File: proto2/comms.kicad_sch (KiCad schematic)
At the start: 35 parts

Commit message: Changes suggested by CFL.
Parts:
- C100, C101, C102, C103, C86, C87, C88, C89, C90, C91, C92, C93, C94, C95, C96, C97, C98, C99: renamed from C?; footprint (none) -> Capacitor_SMD:C_0805_2012Metric; LCSC (none) -> C440198
- U17: renamed from U?; Manufacturer (none) -> Texas Instruments; Part Number (none) -> ISO1540DR
- U18, U19, U20: renamed from U?; Manufacturer (none) -> Novosense; Part Number (none) -> NSI8021N-DSPR
- gave numbers to parts that had none: 13
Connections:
- net 3V3_I2C: now also R138.1
- net +5V renamed +5VP
- net +5VP: no longer C101.1, C93.1, C97.1, U18.1 (VDD1), U19.1 (VDD1), U20.1 (VDD1)
- new net +3V3: C101.1, C93.1, U18.1 (VDD1), U19.1 (VDD1), U20.1 (VDD1)

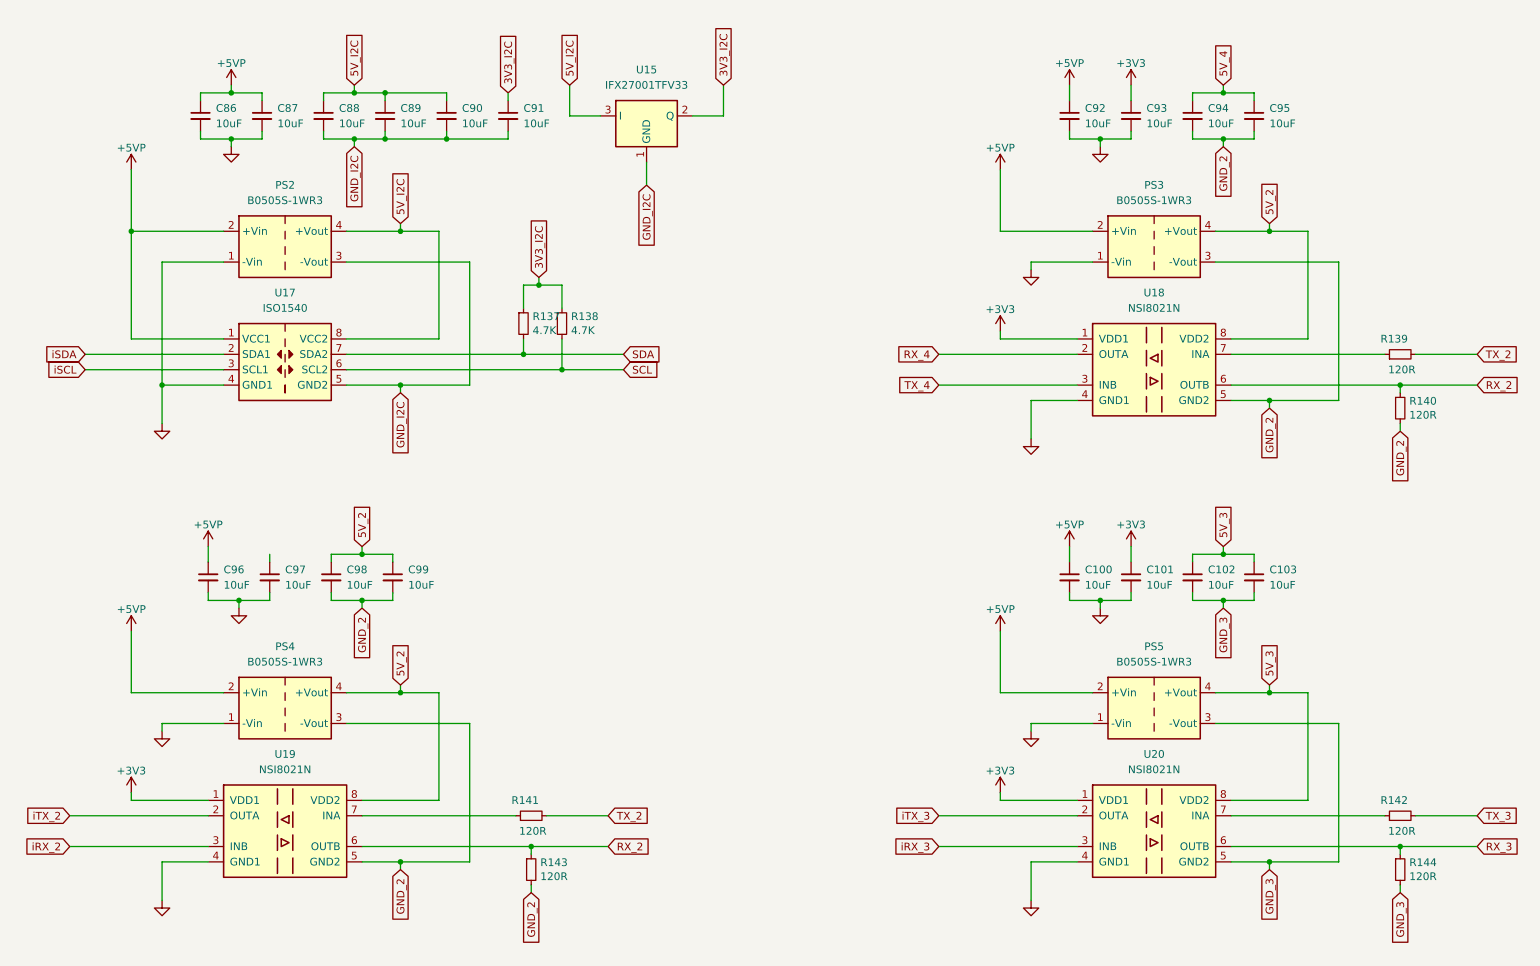
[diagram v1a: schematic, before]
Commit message: Laying out new filters and some schematic updates.
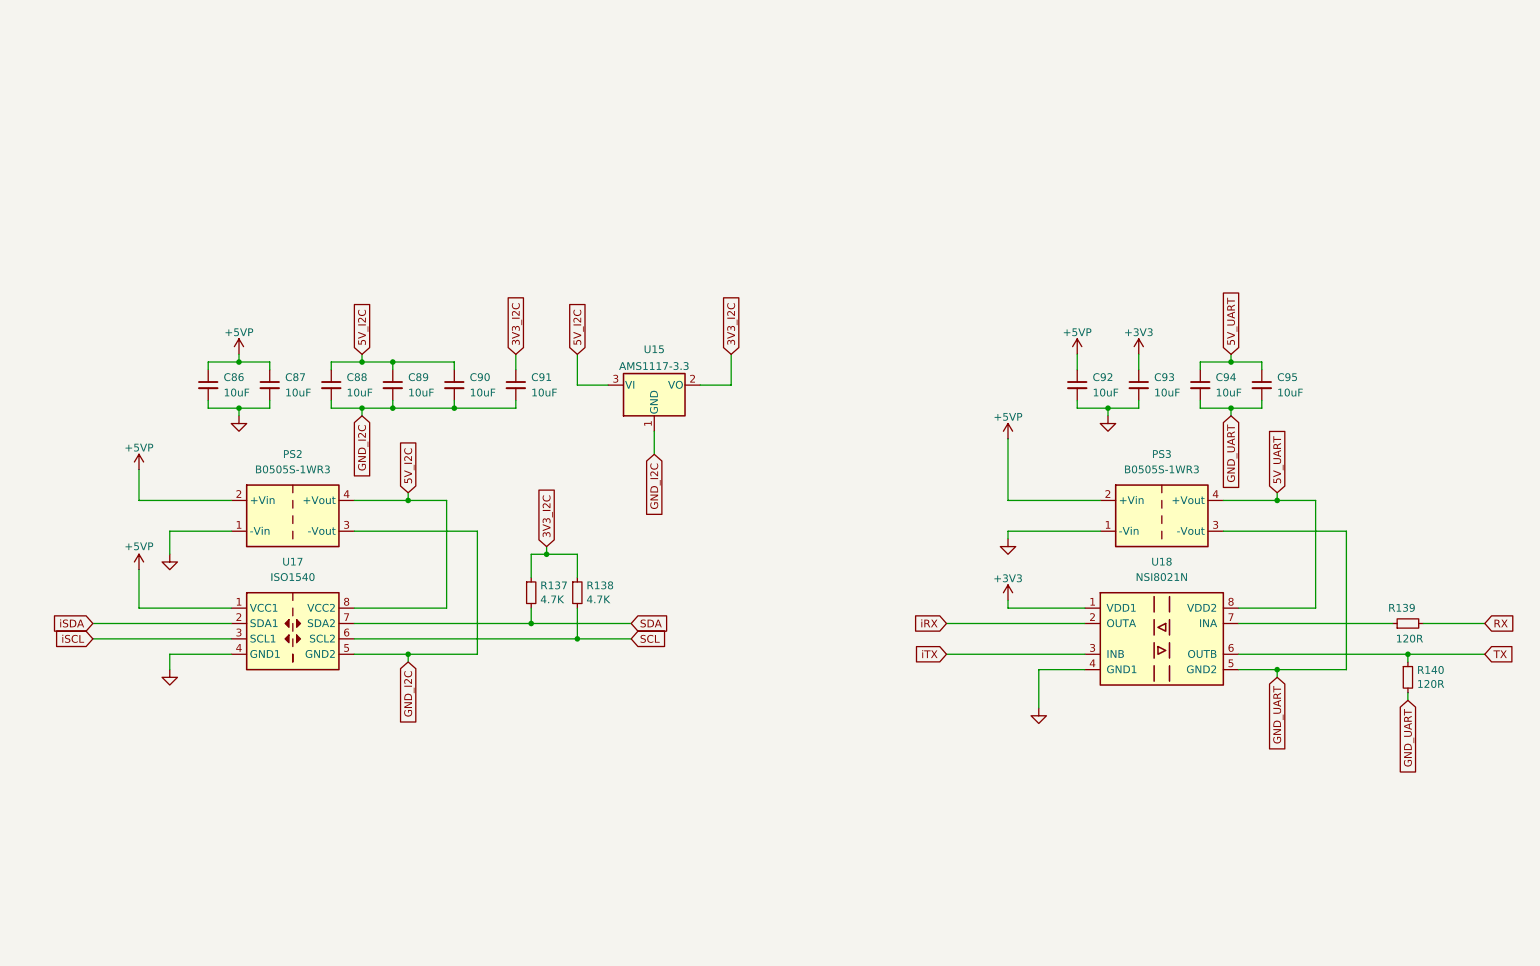
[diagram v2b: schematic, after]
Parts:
- removed C100, C101, C102, C103, C96, C97, C98, C99: 10uF, Capacitor_SMD:C_0805_2012Metric, symbol Device:C_Small
- removed PS4, PS5: B0505S-1WR3, Converter_DCDC:Converter_DCDC_Murata_MEE1SxxxxSC_THT, symbol Converter_DCDC:MEE1S0303SC
- removed R141, R142, R143, R144: 120R, Resistor_SMD:R_0805_2012Metric, symbol Device:R_Small
- removed U15: IFX27001TFV33, Package_TO_SOT_SMD:TO-252-3_TabPin2, symbol Regulator_Linear:IFX27001TFV33
- removed U19, U20: NSI8021N, Package_SO:SOIC-8_3.9x4.9mm_P1.27mm, symbol BCR:NSI8021N
- added U15: AMS1117-3.3, Package_TO_SOT_SMD:SOT-223-3_TabPin2, symbol Regulator_Linear:AMS1117-3.3
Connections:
- net 5V_4 is gone; now on net 5V_UART: C94.1, C95.1
- net 3V3_I2C: now also U15.2 (VO)
- net 5V_I2C: now also U15.3 (VI)
- net GND_I2C: now also U15.1 (GND)
- net 5V_2 renamed 5V_UART
- net GND renamed GND-SIG
- net GND_2 renamed GND_UART
- net RX_2 renamed TX
- net RX_4 renamed iRX
- net TX_2 renamed RX
- net TX_4 renamed iTX
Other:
- company: (none) -> Langhe Greenhaus
- title: (none) -> Greenhouse 2.0 IO Board
- moved on the sheet: C86, C87, C88, C89, C90, C91, C92, C93, C94, C95, PS2, PS3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

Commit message: Final layout for 0.2.0 and various BOM and minor schematic updates.
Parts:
- PS2, PS3: Manufacturer (none) -> Mornsun; Part Number (none) -> B0505S-1WR3
- U15: footprint Package_TO_SOT_SMD:SOT-223-3_TabPin2 -> JLCPCB:SOT-223-3; symbol Regulator_Linear:AMS1117-3.3 -> JLCPCB:AMS1117
- U17: footprint Package_SO:SOIC-8_3.9x4.9mm_P1.27mm -> JLCPCB:SOIC-8_5.4mm_1.27mm; symbol Isolator:ISO1540 -> JLCPCB:Taxas_ISO1540DR
- U18: footprint Package_SO:SOIC-8_3.9x4.9mm_P1.27mm -> JLCPCB:SOIC-8_5.4mm_1.27mm; symbol BCR:NSI8021N -> JLCPCB:Novosense_NSI8021N1-DSPR
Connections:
- no-connect marks 0 -> 1
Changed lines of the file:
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@@
   (junction (at 85.09 68.58) (diameter 0) (color 0 0 0 0)
   )
+  (no_connect (at 135.89 74.93))
   (wire (pts (xy 54.61 68.58) (xy 59.69 68.58))
     (stroke (width 0) (type default) (color 0 0 0 0))
@@
     (pin "2")
   )
-  (symbol (lib_id "Isolator:ISO1540") (at 68.58 111.76 0) (unit 1)
-    (in_bom yes) (on_board yes) (fields_autoplaced)
-    (property "Reference" "U17" (id 0) (at 68.58 101.6 0))
-    (property "Value" "ISO1540" (id 1) (at 68.58 104.14 0))
-    (property "Footprint" "Package_SO:SOIC-8_3.9x4.9mm_P1.27mm" (id 2) (at 68.58 120.65 0)
-      (effects (font (size 1.27 1.27)) hide)
-    )
-    (property "Datasheet" "https://datasheet.lcsc.com/lcsc/1811082013_Texas-Instruments-ISO1540DR_C179739.pdf" (id 3) (at 68.58 110.49 0)
-      (effects (font (size 1.27 1.27)) hide)
-    )
-    (property "LCSC" "C179739" (id 4) (at 68.58 111.76 0)
+  (symbol (lib_id "JLCPCB:Taxas_ISO1540DR") (at 68.58 111.76 0) (unit 1)
+    (in_bom yes) (on_board yes) (fields_autoplaced)
+    (property "Reference" "U17" (id 0) (at 68.58 102.9802 0))
+    (property "Value" "ISO1540" (id 1) (at 68.58 105.5171 0))
+    (property "Footprint" "JLCPCB:SOIC-8_5.4mm_1.27mm" (id 2) (at 68.58 120.65 0)
+      (effects (font (size 1.27 1.27)) hide)
+    )
+    (property "Datasheet" "https://datasheet.lcsc.com/lcsc/1811082013_Texas-Instruments-ISO1540DR_C179739.pdf" (id 3) (at 68.58 123.19 0)
+      (effects (font (size 1.27 1.27)) hide)
+    )
+    (property "LCSC" "C179739" (id 4) (at 68.58 125.73 0)
       (effects (font (size 1.27 1.27)) hide)
     )
@@
     )
     (property "Part Number" "ISO1540DR" (id 6) (at 68.58 111.76 0)
+      (effects (font (size 1.27 1.27)) hide)
+    )
+    (property "MPN" "" (id 7) (at 68.58 111.76 0)
+      (effects (font (size 1.27 1.27)) hide)
+    )
+    (property "JLC" "" (id 8) (at 68.58 111.76 0)
       (effects (font (size 1.27 1.27)) hide)
     )
@@
       (effects (font (size 1.27 1.27)) hide)
     )
+    (property "Manufacturer" "Mornsun" (id 5) (at 68.58 93.98 0)
+      (effects (font (size 1.27 1.27)) hide)
+    )
+    (property "Part Number" "B0505S-1WR3" (id 6) (at 68.58 93.98 0)
+      (effects (font (size 1.27 1.27)) hide)
+    )
     (pin "1")
     (pin "2")
@@
       (effects (font (size 1.27 1.27)) hide)
     )
+    (property "Manufacturer" "Mornsun" (id 5) (at 212.09 93.98 0)
+      (effects (font (size 1.27 1.27)) hide)
+    )
+    (property "Part Number" "B0505S-1WR3" (id 6) (at 212.09 93.98 0)
+      (effects (font (size 1.27 1.27)) hide)
+    )
     (pin "1")
     (pin "2")
@@
     (pin "1")
   )
-  (symbol (lib_id "BCR:NSI8021N") (at 212.09 114.3 0) (unit 1)
+  (symbol (lib_id "JLCPCB:Novosense_NSI8021N1-DSPR") (at 212.09 114.3 0) (unit 1)
     (in_bom yes) (on_board yes) (fields_autoplaced)
     (property "Reference" "U18" (id 0) (at 212.09 101.6 0))
     (property "Value" "NSI8021N" (id 1) (at 212.09 104.14 0))
-    (property "Footprint" "Package_SO:SOIC-8_3.9x4.9mm_P1.27mm" (id 2) (at 212.09 124.46 0)
+    (property "Footprint" "JLCPCB:SOIC-8_5.4mm_1.27mm" (id 2) (at 212.09 125.73 0)
       (effects (font (size 1.27 1.27) italic) hide)
     )
-    (property "Datasheet" "https://datasheet.lcsc.com/lcsc/2012231310_NOVOSENSE-NSI8021N1-DSPR_C917451.pdf" (id 3) (at 212.09 127 0)
-      (effects (font (size 1.27 1.27)) hide)
-    )
-    (property "LCSC" "C917451" (id 4) (at 212.09 129.54 0)
+    (property "Datasheet" "https://datasheet.lcsc.com/lcsc/2012231310_NOVOSENSE-NSI8021N1-DSPR_C917451.pdf" (id 3) (at 212.09 128.27 0)
+      (effects (font (size 1.27 1.27)) hide)
+    )
+    (property "LCSC" "C917451" (id 4) (at 212.09 130.81 0)
       (effects (font (size 1.27 1.27)) hide)
     )
@@
     )
     (property "Part Number" "NSI8021N-DSPR" (id 6) (at 212.09 114.3 0)
+      (effects (font (size 1.27 1.27)) hide)
+    )
+    (property "MPN" "" (id 7) (at 212.09 114.3 0)
+      (effects (font (size 1.27 1.27)) hide)
+    )
+    (property "JLC" "" (id 8) (at 212.09 114.3 0)
       (effects (font (size 1.27 1.27)) hide)
     )
@@
     (pin "8")
   )
-  (symbol (lib_id "Regulator_Linear:AMS1117-3.3") (at 128.27 72.39 0) (unit 1)
+  (symbol (lib_id "JLCPCB:AMS1117") (at 128.27 72.39 0) (unit 1)
     (in_bom yes) (on_board yes) (fields_autoplaced)
     (property "Reference" "U15" (id 0) (at 128.27 66.5185 0))
     (property "Value" "AMS1117-3.3" (id 1) (at 128.27 69.2936 0))
-    (property "Footprint" "Package_TO_SOT_SMD:SOT-223-3_TabPin2" (id 2) (at 128.27 67.31 0)
-      (effects (font (size 1.27 1.27)) hide)
-    )
-    (property "Datasheet" "http://www.advanced-monolithic.com/pdf/ds1117.pdf" (id 3) (at 130.81 78.74 0)
+    (property "Footprint" "JLCPCB:SOT-223-3" (id 2) (at 128.27 67.31 0)
+      (effects (font (size 1.27 1.27)) hide)
+    )
+    (property "Datasheet" "http://www.diodes.com/datasheets/AP1117.pdf" (id 3) (at 130.81 78.74 0)
       (effects (font (size 1.27 1.27)) hide)
     )
@@
     (pin "2")
     (pin "3")
+    (pin "4")
   )
   (symbol (lib_id "Device:C_Small") (at 228.6 72.39 0) (unit 1)
